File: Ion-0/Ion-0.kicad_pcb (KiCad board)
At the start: 4 copper layers, 54.6 x 86.4 mm, 107 parts, among them J1 Beaglebone-green-P9, J10 Conn_CAN, J13 Conn_01x04, J15 Conn_01x04, J2 Beaglebone-green-P8, J3 Conn_02x06_Odd_Even, J4 Conn_02x06_Odd_Even, J5 Conn_02x06_Odd_Even, J6 Coaxial_Small, J7 Conn_Probs, J8 Conn_Heater, Q1 IRLML6244, Q2 IRLML6244, U1 HDC2080, U2 MS5607-02BA, U3 BNO085, U4 TCA9617ADGKR, U5 A4988SETTR-T, U6 MAX-M10M-00B, U7 TPS3850H50DRCR, U8 SN65HVD230, Y2 9HT10-32.768KBZF-T

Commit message: added production files
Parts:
- moved R19 1.45 mm to (156.1, 134.7)
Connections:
- U7 pad V: (no net) -> GND
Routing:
- net +3V3: track 90.5 -> 91.7 mm
- net /~{STP-SLP}: track 39.7 -> 39.0 mm
- net GND: vias 199 -> 202

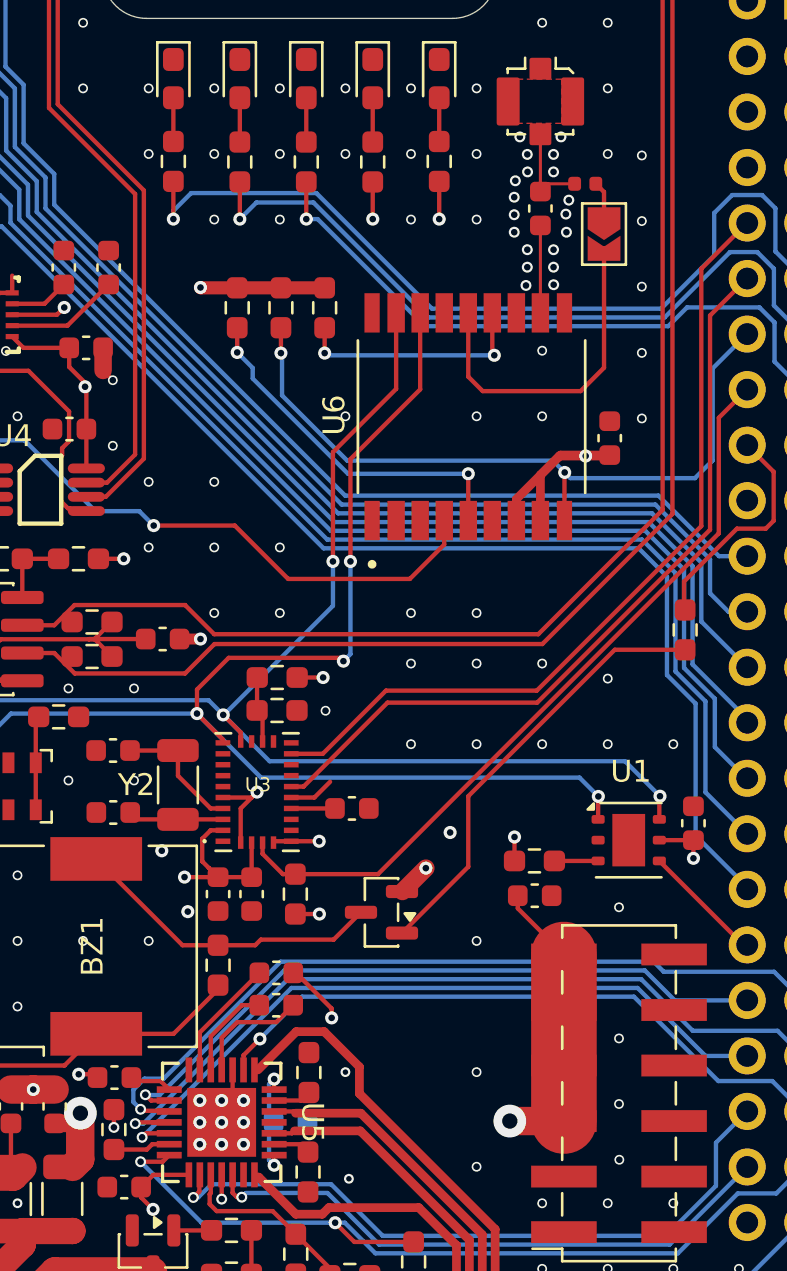
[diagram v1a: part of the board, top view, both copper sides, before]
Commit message: fixed impedance mismatch
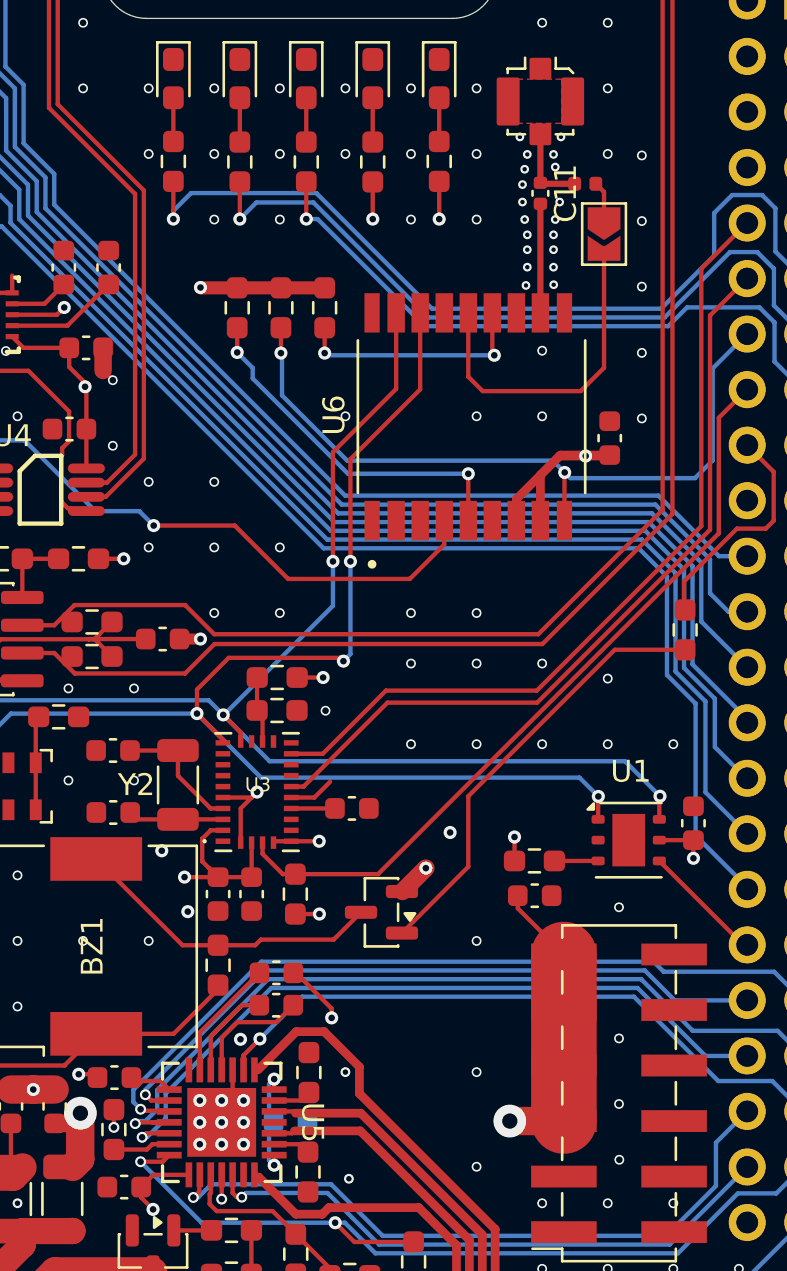
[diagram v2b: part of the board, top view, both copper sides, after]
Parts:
- C11: footprint Capacitor_SMD:C_0603_1608Metric -> Capacitor_SMD:C_0402_1005Metric
- moved C11 0.70 mm to (161.9, 85.8)
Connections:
- U7 pad V: GND -> (no net)
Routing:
- net Net-(U6-RF_IN): track 4.00 -> 4.99 mm
- net /~{STP-RST}: track 33.4 -> 34.1 mm
- net /STP-MS3: track 37.1 -> 37.7 mm
- net Net-(J6-In): track 4.33 -> 3.80 mm
- net GND: vias 202 -> 203

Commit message: new production files
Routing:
- net GND: vias 203 -> 206

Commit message: BOM ORDER
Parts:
- removed R12: 523, Resistor_SMD:R_0603_1608Metric_Pad0.98x0.95mm_HandSolder
- removed R13: 80.6, Resistor_SMD:R_0603_1608Metric_Pad0.98x0.95mm_HandSolder
- J15, J7: footprint Connector_JST:JST_XH_B4B-XH-AM_1x04_P2.50mm_Vertical -> TerminalBlock:TerminalBlock_Xinya_XY308-2.54-4P_1x04_P2.54mm_Horizontal
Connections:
- U7 pad 10: Net-(U7-SENSE) -> +5V
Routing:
- net Net-(U7-SENSE): track 4.15 -> 0.00 mm
- net +5V: track 57.0 -> 60.1 mm, vias 6 -> 7
